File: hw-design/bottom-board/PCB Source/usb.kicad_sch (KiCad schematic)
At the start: 17 parts, among them J11 USB_B, J12 USB_A, U16 TPS2041B

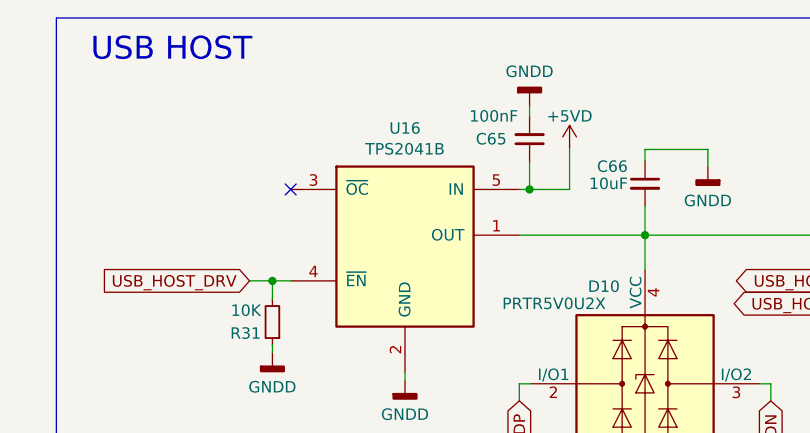
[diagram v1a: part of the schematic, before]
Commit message: mainboard: correct CC TX pin + update fabrication files
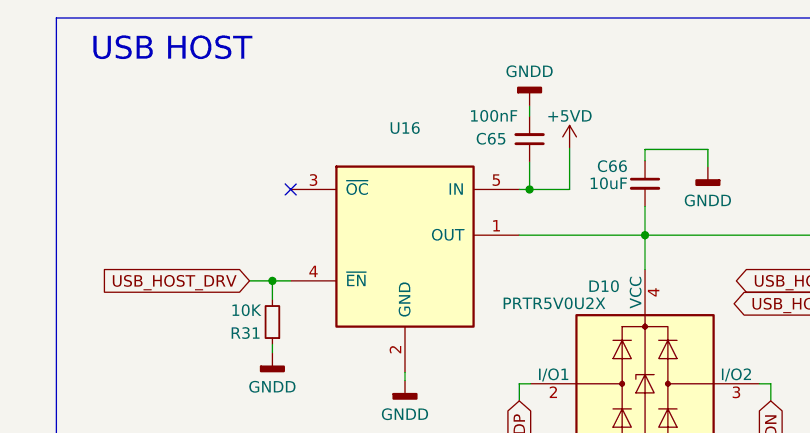
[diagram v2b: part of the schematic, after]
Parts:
- U16: value TPS2041B -> (none); footprint Package_TO_SOT_SMD:SOT-23-5 -> (none); MPN (none) -> TPS2041B
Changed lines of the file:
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@@
     (in_bom yes) (on_board yes)
     (property "Reference" "U16" (id 0) (at 192.405 66.8782 0))
-    (property "Value" "TPS2041B" (id 1) (at 192.405 69.1896 0))
-    (property "Footprint" "Package_TO_SOT_SMD:SOT-23-5" (id 2) (at 192.405 66.04 0)
+    (property "Value" "" (id 1) (at 192.405 69.1896 0))
+    (property "Footprint" "" (id 2) (at 192.405 66.04 0)
       (effects (font (size 1.27 1.27)) hide)
     )
@@
       (effects (font (size 1.27 1.27)) hide)
     )
+    (property "MPN" "TPS2041B" (id 4) (at 192.405 78.74 0)
+      (effects (font (size 1.524 1.524)) hide)
+    )
     (pin "1")
